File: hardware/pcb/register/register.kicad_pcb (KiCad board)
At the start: 2 copper layers, 62.2 x 21.6 mm, 50 parts, among them J1 Conn_01x08_Male, J2 Conn_01x04_Male, J3 Conn_01x04_Male, J4 Conn_01x04_Male, J5 Conn_01x08_Male, J6 Conn_01x08_Male, U1 74HC245, U2 74HC173, U3 74HC173, U4 74HC173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

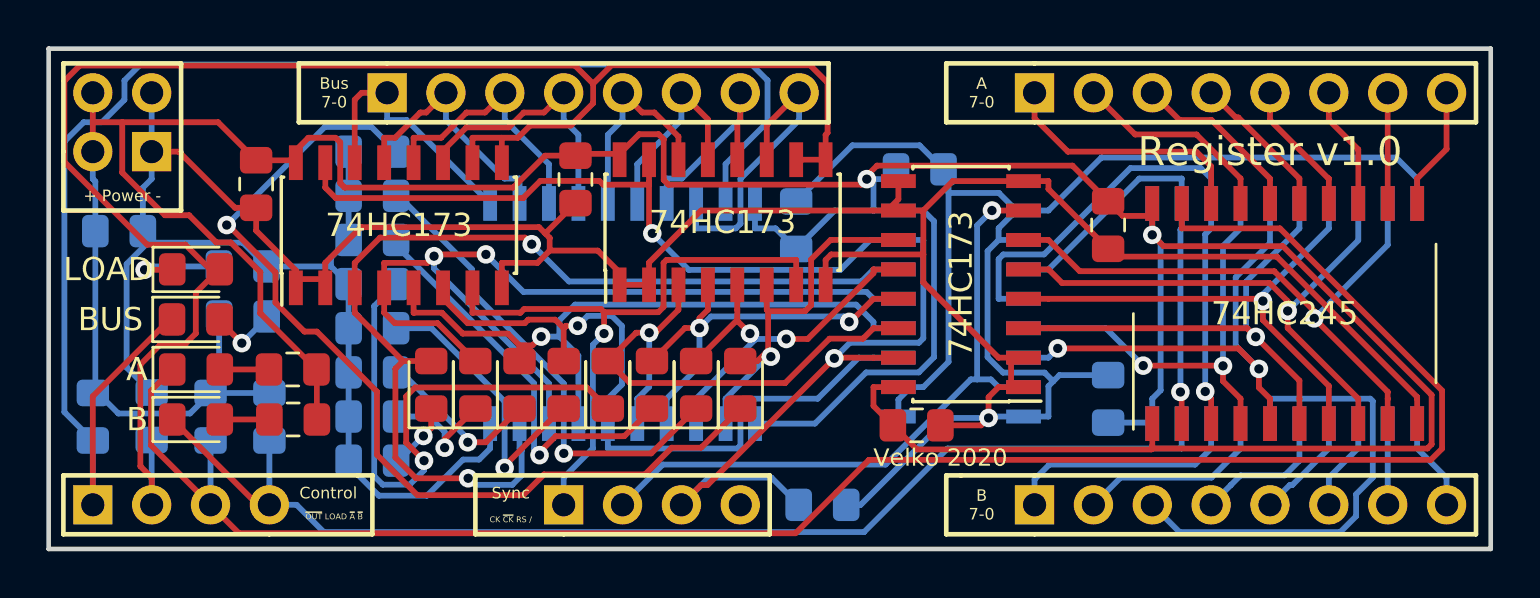
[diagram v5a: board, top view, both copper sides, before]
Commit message: Add copper pours and some silk
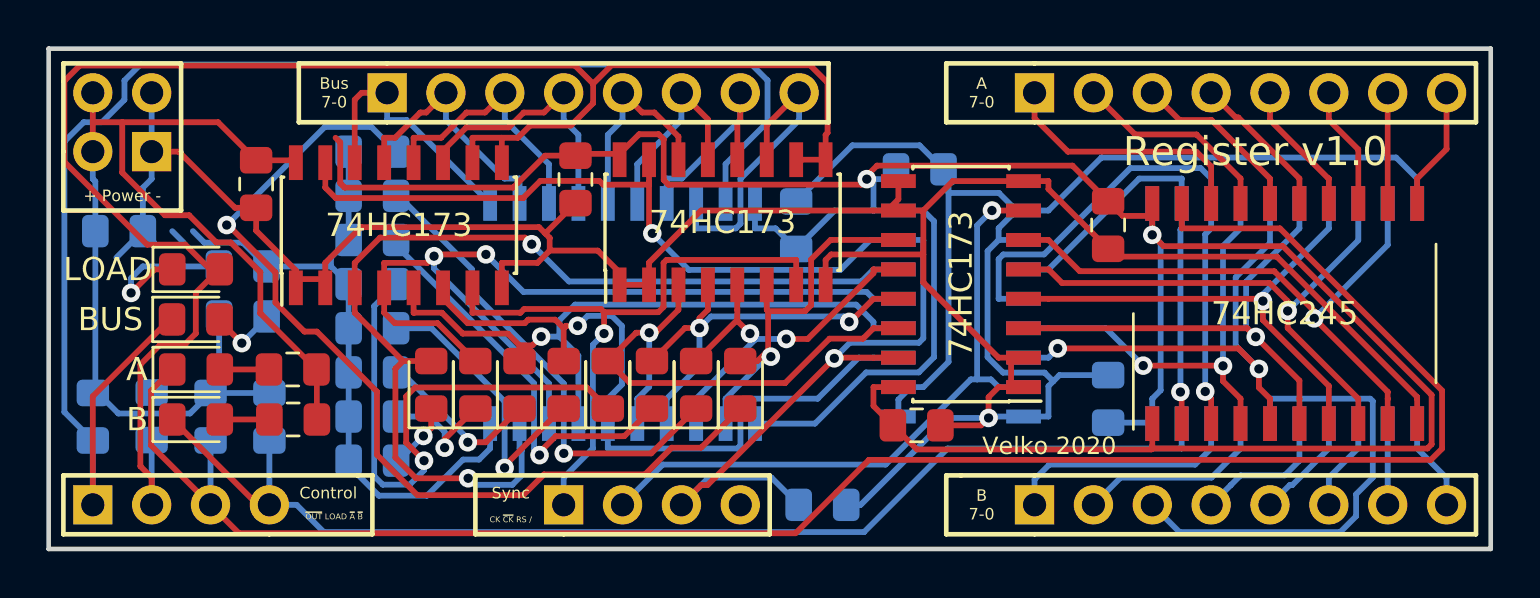
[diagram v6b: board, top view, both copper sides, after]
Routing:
- net GND: track 210.1 -> 203.5 mm
- net Net-(D9-Pad1): track 4.47 -> 6.86 mm
- net VCC: track 181.8 -> 179.8 mm
- added copper zone on B.Cu, net GND
- added copper zone on F.Cu, net VCC
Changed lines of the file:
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@@
   (general
     (thickness 1.6)
-    (drawings 52)
+    (drawings 60)
     (tracks 812)
     (zones 0)
@@
   (layers
     (0 F.Cu signal hide)
-    (31 B.Cu signal)
+    (31 B.Cu signal hide)
     (32 B.Adhes user hide)
     (33 F.Adhes user hide)
     (34 B.Paste user hide)
     (35 F.Paste user hide)
-    (36 B.SilkS user hide)
+    (36 B.SilkS user)
     (37 F.SilkS user hide)
-    (38 B.Mask user hide)
+    (38 B.Mask user)
     (39 F.Mask user hide)
     (40 Dwgs.User user hide)
@@
     (last_trace_width 0.25)
     (trace_clearance 0.2)
-    (zone_clearance 0.508)
+    (zone_clearance 0.254)
     (zone_45_only no)
     (trace_min 0.2)
@@
       (effects (font (size 1 1) (thickness 0.15)) (justify mirror))
     )
-    (fp_text value 10K (at 0 -1.65 270) (layer B.Fab)
+    (fp_text value 10K (at -3.311 -1.397) (layer B.SilkS)
       (effects (font (size 1 1) (thickness 0.15)) (justify mirror))
     )
@@
       (effects (font (size 1 1) (thickness 0.15)) (justify mirror))
     )
-    (fp_text value 330 (at 0 -1.65 180) (layer B.Fab)
+    (fp_text value 330 (at -1.025 2.921 180) (layer B.SilkS)
       (effects (font (size 1 1) (thickness 0.15)) (justify mirror))
     )
@@
     )
   )
+  (gr_line (start 41.148 46.99) (end 35.814 46.99) (layer B.SilkS) (width 0.2))
+  (gr_line (start 46.355 54.991) (end 46.99 54.991) (layer B.SilkS) (width 0.2))
+  (gr_line (start 46.355 49.149) (end 46.355 54.991) (layer B.SilkS) (width 0.2))
+  (gr_line (start 41.148 49.149) (end 46.355 49.149) (layer B.SilkS) (width 0.2))
+  (gr_line (start 41.148 39.751) (end 41.148 49.149) (layer B.SilkS) (width 0.2))
+  (gr_line (start 51.308 39.751) (end 41.148 39.751) (layer B.SilkS) (width 0.2))
+  (gr_line (start 51.308 54.991) (end 51.308 39.751) (layer B.SilkS) (width 0.2))
+  (gr_line (start 46.99 54.991) (end 51.308 54.991) (layer B.SilkS) (width 0.2))
   (gr_line (start 40.64 36.83) (end 40.64 40.64) (layer F.SilkS) (width 0.2))
   (gr_line (start 35.56 36.83) (end 40.64 36.83) (layer F.SilkS) (width 0.2))
@@
     (effects (font (size 0.5 0.5) (thickness 0.1)))
   )
-  (gr_text "Velko 2020" (at 73.406 53.848) (layer F.SilkS)
+  (gr_text "Velko 2020" (at 78.105 53.34) (layer F.SilkS)
     (effects (font (size 0.75 0.75) (thickness 0.1875)))
   )
-  (gr_text "Register v1.0" (at 87.63 40.64) (layer F.SilkS)
+  (gr_text "Register v1.0" (at 86.995 40.64) (layer F.SilkS)
     (effects (font (size 1.25 1.25) (thickness 0.3)))
   )
@@
   (segment (start 47.5076 41.9997) (end 47.5076 40.2414) (width 0.25) (layer F.Cu) (net 1))
   (segment (start 47.5076 40.2414) (end 47.3058 40.0396) (width 0.25) (layer F.Cu) (net 1))
-  (segment (start 47.3058 40.0396) (end 46.1307 40.0396) (width 0.25) (layer F.Cu) (net 1))
-  (segment (start 46.1307 40.0396) (end 45.593 40.5773) (width 0.25) (layer F.Cu) (net 1))
   (segment (start 59.563 40.734) (end 57.7365 40.734) (width 0.25) (layer F.Cu) (net 1))
   (segment (start 57.7365 40.734) (end 57.658 40.8125) (width 0.25) (layer F.Cu) (net 1))
@@
   (segment (start 47.108 45.212) (end 47.87 44.45) (width 0.25) (layer B.Cu) (net 2))
   (segment (start 39.3467 44.4266) (end 39.4866 44.5666) (width 0.25) (layer B.Cu) (net 2))
-  (segment (start 39.4866 44.5666) (end 43.2966 44.5666) (width 0.25) (layer B.Cu) (net 2))
   (segment (start 43.2966 44.5666) (end 44.323 45.593) (width 0.25) (layer B.Cu) (net 2))
   (segment (start 56.3539 44.1666) (end 56.0851 43.8979) (width 0.25) (layer F.Cu) (net 2))
@@
   (segment (start 39.37 38.1) (end 39.37 40.64) (width 0.25) (layer B.Cu) (net 2))
   (segment (start 38.989 44.069) (end 39.3467 44.4266) (width 0.25) (layer B.Cu) (net 2))
-  (segment (start 39.3467 44.4266) (end 38.2881 45.4852) (width 0.25) (layer B.Cu) (net 2))
-  (segment (start 38.2881 45.4852) (end 38.2881 49.9541) (width 0.25) (layer B.Cu) (net 2))
-  (segment (start 38.2881 49.9541) (end 39.37 51.036) (width 0.25) (layer B.Cu) (net 2))
   (segment (start 93.98 42.875) (end 93.98 41.7997) (width 0.25) (layer B.Cu) (net 2))
   (segment (start 76.995 43.18) (end 78.0703 43.18) (width 0.25) (layer B.Cu) (net 2))
@@
   (via (at 75.485 52.1312) (size 0.8) (layers F.Cu B.Cu) (net 2))
   (segment (start 59.563 46.388) (end 60.833 46.388) (width 0.25) (layer F.Cu) (net 2))
+  (segment (start 38.989 44.069) (end 37.846 45.212) (width 0.25) (layer B.Cu) (net 2))
+  (segment (start 40.7566 44.5666) (end 40.259 44.069) (width 0.25) (layer B.Cu) (net 2))
+  (segment (start 43.2966 44.5666) (end 41.6456 44.5666) (width 0.25) (layer B.Cu) (net 2))
+  (segment (start 41.6456 44.5666) (end 41.148 44.069) (width 0.25) (layer B.Cu) (net 2))
   (segment (start 42.609 43.8069) (end 42.6669 43.8069) (width 0.25) (layer F.Cu) (net 3))
   (segment (start 42.6669 43.8069) (end 44.7132 45.8532) (width 0.25) (layer F.Cu) (net 3))
@@
   (via (at 51.0969 52.9087) (size 0.8) (layers F.Cu B.Cu) (net 42))
   (segment (start 40.259 45.72) (end 40.2426 45.7364) (width 0.25) (layer F.Cu) (net 43))
-  (segment (start 40.2426 45.7364) (end 39.064 45.7364) (width 0.25) (layer F.Cu) (net 43))
-  (segment (start 42.273 45.593) (end 39.2074 45.593) (width 0.25) (layer B.Cu) (net 43))
-  (segment (start 39.2074 45.593) (end 39.064 45.7364) (width 0.25) (layer B.Cu) (net 43))
-  (via (at 39.064 45.7364) (size 0.8) (layers F.Cu B.Cu) (net 43))
+  (via (at 38.481 46.736) (size 0.8) (layers F.Cu B.Cu) (net 43))
+  (segment (start 39.497 45.72) (end 38.481 46.736) (width 0.25) (layer F.Cu) (net 43))
+  (segment (start 40.259 45.72) (end 39.497 45.72) (width 0.25) (layer F.Cu) (net 43))
+  (segment (start 38.481 46.736) (end 38.481 46.101) (width 0.25) (layer B.Cu) (net 43))
+  (segment (start 38.989 45.593) (end 42.273 45.593) (width 0.25) (layer B.Cu) (net 43))
+  (segment (start 38.481 46.101) (end 38.989 45.593) (width 0.25) (layer B.Cu) (net 43))
   (segment (start 39.37 55.88) (end 39.37 53.086) (width 0.25) (layer B.Cu) (net 44))
   (segment (start 58.42 37.7072) (end 57.6374 36.9246) (width 0.25) (layer F.Cu) (net 44))
@@
   (segment (start 76.995 44.45) (end 78.0703 44.45) (width 0.25) (layer F.Cu) (net 62))
   (via (at 89.5401 47.8355) (size 0.8) (layers F.Cu B.Cu) (net 62))
+  (zone (net 2) (net_name GND) (layer B.Cu) (hatch edge 0.508)
+    (connect_pads (clearance 0.254))
+    (min_thickness 0.254)
+    (fill yes (arc_segments 16) (thermal_gap 0.508) (thermal_bridge_width 0.508))
+    (polygon
+      (pts
+        (xy 34.925 36.195) (xy 97.155 36.195) (xy 97.155 57.785) (xy 34.925 57.785) (xy 34.925 57.15)
+      )
+    )
+  )
+  (zone (net 1) (net_name VCC) (layer F.Cu) (hatch edge 0.508)
+    (connect_pads (clearance 0.254))
+    (min_thickness 0.254)
+    (fill yes (arc_segments 16) (thermal_gap 0.508) (thermal_bridge_width 0.508))
+    (polygon
+      (pts
+        (xy 34.925 36.195) (xy 97.155 36.195) (xy 97.155 57.785) (xy 34.925 57.785)
+      )
+    )
+  )
 )

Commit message: Fix - LOAD should be active-low
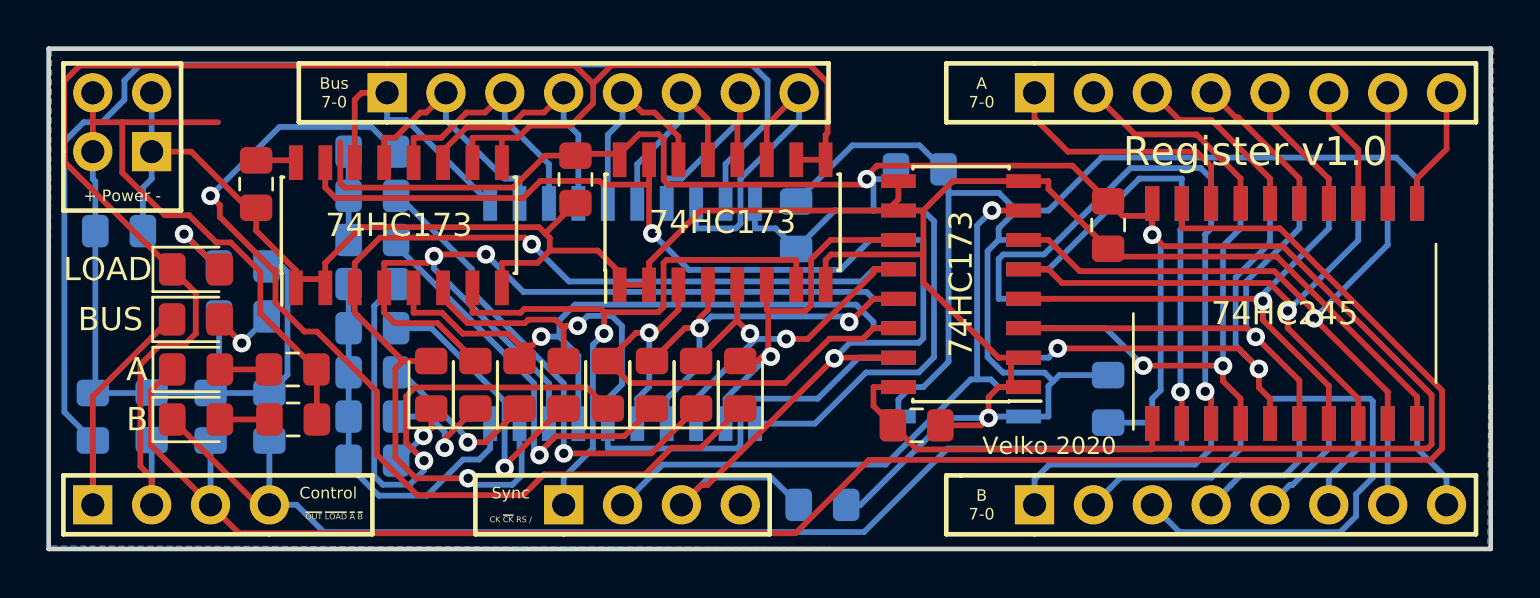
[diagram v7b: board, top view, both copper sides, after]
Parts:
- turned R3 to 90 degrees
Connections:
- D9 pad 1: Net-(D9-Pad1) -> ~LOAD~
- D9 pad 2: LOAD -> Net-(D9-Pad2)
- J2 pad 2: LOAD -> ~LOAD~
- R17 pad 1: GND -> VCC
- R17 pad 2: Net-(D9-Pad1) -> Net-(D9-Pad2)
- R3 pad 1: GND -> ~LOAD~
- R3 pad 2: LOAD -> VCC
- U2 pad 10: LOAD -> ~LOAD~
- U2 pad 9: LOAD -> ~LOAD~
- U4 pad 10: LOAD -> ~LOAD~
- U4 pad 9: LOAD -> ~LOAD~
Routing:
- net LOAD: track 74.8 -> 0.00 mm
- net ~LOAD~: track 0.00 -> 72.9 mm
- net GND: track 203.5 -> 191.9 mm
- net Net-(D9-Pad1): track 6.86 -> 0.00 mm, vias 1 -> 0
- net Net-(D9-Pad2): track 0.00 -> 4.57 mm, vias 0 -> 1
- net VCC: track 179.8 -> 183.3 mm
- net Net-(D1-Pad1): track 40.4 -> 42.2 mm
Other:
- board text added: "~OUT~ ~LOAD~ ~A~ ~B~"
- board text removed: "~OUT~ LOAD ~A~ ~B~"
